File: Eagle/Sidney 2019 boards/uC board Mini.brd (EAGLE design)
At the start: 100 x 100 mm, 55 parts

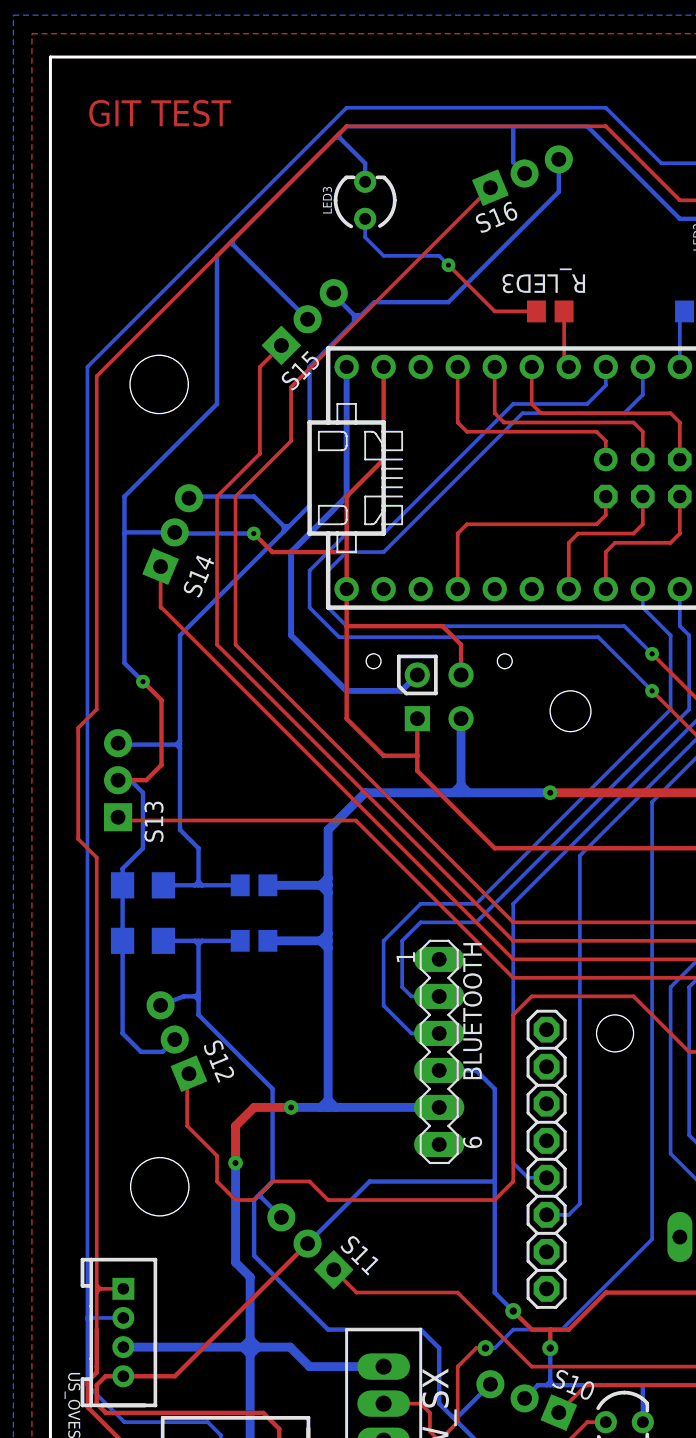
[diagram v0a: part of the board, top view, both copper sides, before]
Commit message: slight improvements on the top PCB
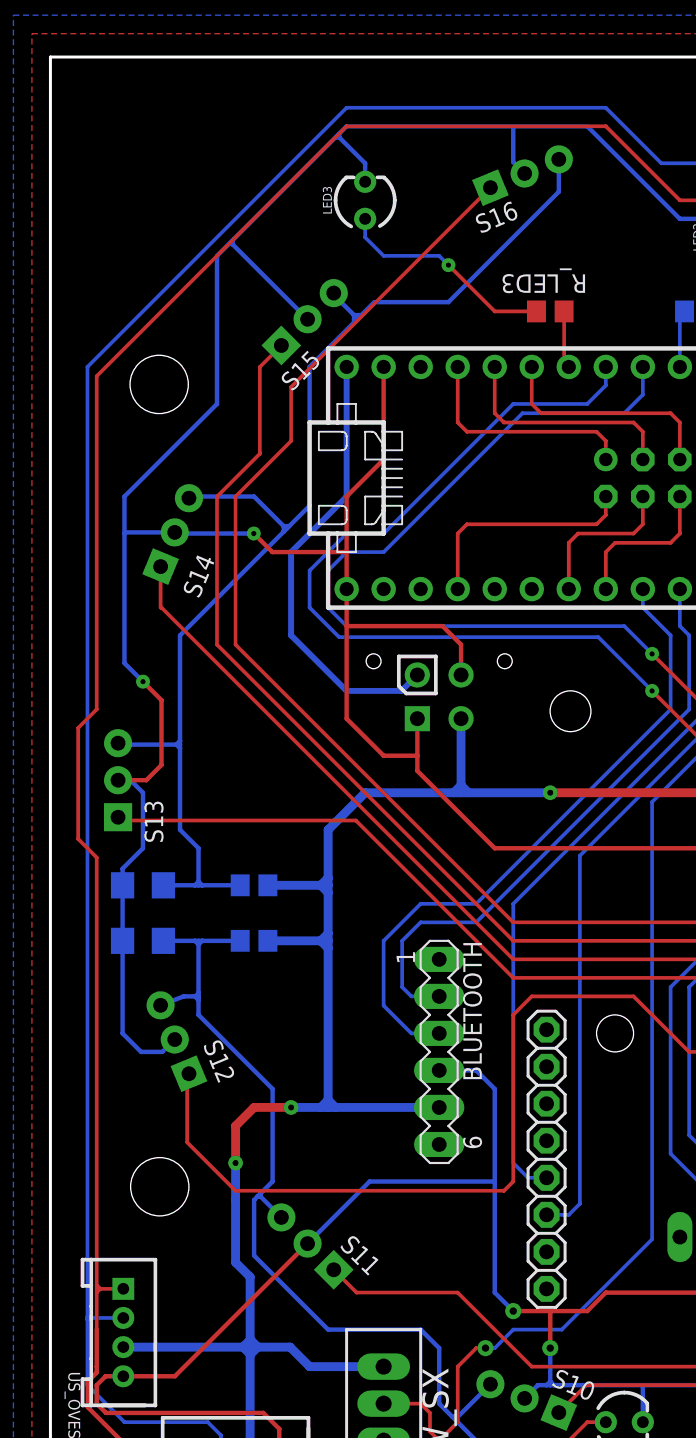
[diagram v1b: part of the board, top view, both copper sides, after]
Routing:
- net SP12: track 86.2 -> 84.3 mm
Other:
- board text removed: "GIT TEST"
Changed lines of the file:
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@@
 <text x="31.75" y="49.53" size="1.778" layer="26" rot="MR0">SUPPLY_CON</text>
 <text x="64.77" y="64.77" size="1.778" layer="25">TEENSY 3.5</text>
-<text x="2.54" y="95.25" size="1.778" layer="1">GIT TEST</text>
 </plain>
 <attributes>
@@
 <wire x1="30.48" y1="15.24" x2="31.75" y2="13.97" width="0.3048" layer="16"/>
 <via x="31.75" y="13.97" extent="1-16" drill="0.5"/>
-<wire x1="31.75" y1="13.97" x2="33.02" y2="12.7" width="0.3048" layer="1"/>
 <wire x1="50.8" y1="19.05" x2="50.8" y2="15.24" width="0.3048" layer="1"/>
 <wire x1="30.48" y1="22.86" x2="30.48" y2="15.24" width="0.3048" layer="16"/>
-<wire x1="35.56" y1="12.7" x2="34.29" y2="12.7" width="0.3048" layer="1"/>
-<wire x1="34.29" y1="12.7" x2="33.02" y2="12.7" width="0.3048" layer="1"/>
 <wire x1="66.294" y1="15.494" x2="66.04" y2="15.24" width="0.3048" layer="1"/>
 <wire x1="66.04" y1="15.24" x2="60.96" y2="15.24" width="0.3048" layer="1"/>
 <wire x1="60.96" y1="15.24" x2="50.8" y2="15.24" width="0.3048" layer="1"/>
-<wire x1="38.1" y1="15.24" x2="35.56" y2="12.7" width="0.3048" layer="1"/>
+<wire x1="38.1" y1="15.24" x2="36.83" y2="13.97" width="0.3048" layer="1"/>
 <wire x1="50.8" y1="15.24" x2="38.1" y2="15.24" width="0.3048" layer="1"/>
-<wire x1="34.29" y1="12.7" x2="34.29" y2="11.43" width="0.3048" layer="1"/>
 <via x="34.29" y="11.43" extent="1-16" drill="0.5"/>
 <wire x1="34.29" y1="11.43" x2="34.29" y2="9.144" width="0.3048" layer="16"/>
@@
 <vertex x="-2.54" y="-1.27"/>
 </polygon>
+<wire x1="31.75" y1="13.97" x2="34.29" y2="13.97" width="0.3048" layer="1"/>
+<wire x1="34.29" y1="13.97" x2="36.83" y2="13.97" width="0.3048" layer="1"/>
+<wire x1="34.29" y1="11.43" x2="34.29" y2="13.97" width="0.3048" layer="1"/>
 </signal>
 <signal name="SP3">
@@
 <wire x1="54.61" y1="31.75" x2="43.815" y2="31.75" width="0.254" layer="1"/>
 <wire x1="33.02" y1="35.56" x2="31.75" y2="34.29" width="0.254" layer="1"/>
-<wire x1="31.75" y1="34.29" x2="31.75" y2="22.86" width="0.254" layer="1"/>
-<wire x1="31.75" y1="22.86" x2="30.48" y2="21.59" width="0.254" layer="1"/>
-<wire x1="30.48" y1="21.59" x2="19.05" y2="21.59" width="0.254" layer="1"/>
-<wire x1="19.05" y1="21.59" x2="17.78" y2="22.86" width="0.254" layer="1"/>
-<wire x1="17.78" y1="22.86" x2="15.24" y2="22.86" width="0.254" layer="1"/>
+<wire x1="31.75" y1="22.86" x2="31.75" y2="34.29" width="0.254" layer="1"/>
 <wire x1="43.815" y1="31.75" x2="40.005" y2="35.56" width="0.254" layer="1"/>
 <wire x1="40.005" y1="35.56" x2="33.02" y2="35.56" width="0.254" layer="1"/>
-<wire x1="13.97" y1="21.59" x2="15.24" y2="22.86" width="0.254" layer="1"/>
-<wire x1="12.7" y1="21.59" x2="13.97" y2="21.59" width="0.254" layer="1"/>
-<wire x1="9.3824" y1="30.133725" x2="9.50201875" y2="30.25334375" width="0.254" layer="1"/>
-<wire x1="9.3824" y1="30.133725" x2="9.3824" y2="26.67" width="0.254" layer="1"/>
-<wire x1="9.3824" y1="26.67" x2="11.43" y2="24.6224" width="0.254" layer="1"/>
-<wire x1="11.43" y1="24.6224" x2="11.43" y2="22.86" width="0.254" layer="1"/>
-<wire x1="11.43" y1="22.86" x2="12.7" y2="21.59" width="0.254" layer="1"/>
+<wire x1="9.50201875" y1="30.25334375" x2="9.3824" y2="30.133725" width="0.254" layer="1"/>
+<wire x1="31.115" y1="22.225" x2="31.75" y2="22.86" width="0.254" layer="1"/>
+<wire x1="9.3824" y1="30.133725" x2="9.3824" y2="25.5426" width="0.254" layer="1"/>
+<wire x1="9.3824" y1="25.5426" x2="12.7" y2="22.225" width="0.254" layer="1"/>
+<wire x1="12.7" y1="22.225" x2="31.115" y2="22.225" width="0.254" layer="1"/>
 </signal>
 <signal name="SP1">
@@
 <wire x1="90.17" y1="95.885" x2="89.7255" y2="96.3295" width="0.6096" layer="16"/>
 <wire x1="89.7255" y1="96.3295" x2="89.535" y2="96.52" width="0.6096" layer="16"/>
-<wire x1="12.7" y1="17.31" x2="12.7" y2="24.13" width="0.6096" layer="16"/>
+<wire x1="12.7" y1="17.31" x2="12.7" y2="21.59" width="0.6096" layer="16"/>
+<wire x1="12.7" y1="21.59" x2="12.7" y2="24.13" width="0.6096" layer="16"/>
 <wire x1="13.97" y1="27.94" x2="12.7" y2="26.67" width="0.6096" layer="1"/>
 <via x="12.7" y="24.13" extent="1-16" drill="0.4064"/>

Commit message: backup
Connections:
- removed net +5V/1: ARDUINO_PRO_MINI.21, BLUETOOTH.5, IMU_1.1, RB1.1, RB2.1, RB3.1, RB4.1, R_SCL.2, R_SCL1.2, R_SDA.2, R_SDA1.2, SUPPLY_CON.P$2, SW_DX.1, SW_SX.1, U$2.27, US_EST.3, US_NORD.3, US_OVEST.3, US_SUD.3
- new net +5V/S: RB1.1, RB2.1, RB3.1, RB4.1, R_SCL1.2, R_SDA1.2, SUPPLY_CON.P$2, SW_DX.1, SW_SX.1, US_EST.3, US_NORD.3, US_OVEST.3, US_SUD.3
- net +5V: now also ARDUINO_PRO_MINI.21, BLUETOOTH.5, IMU_1.1, R_SCL.2, R_SDA.2, U$2.27
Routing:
- net +5V/1: track 368.8 -> 0.00 mm, vias 10 -> 0
- net +5V/S: track 0.00 -> 350.4 mm, vias 0 -> 10

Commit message: general improvements to the boards
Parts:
- removed SUPPLY_CON: (no value), con-molex-micro-fit-3_0:43045-0412
- added J1: 39-28-1043, 39-28-1043:39-28-1043
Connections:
- net +5V: now also J1.3; no longer SUPPLY_CON.P$3
- net +5V/S: now also J1.2; no longer SUPPLY_CON.P$2
- net GND: now also J1.1, J1.4; no longer SUPPLY_CON.P$1, SUPPLY_CON.P$4
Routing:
- net GND: track 657.9 -> 653.3 mm
- net +5V/S: track 350.4 -> 345.8 mm
- net +5V: track 30.7 -> 29.1 mm
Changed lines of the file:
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@@
 <attribute name="SPICEPREFIX" value="R" x="88.9" y="92.075" size="1.778" layer="27" rot="R90" display="off"/>
 </element>
-<element name="SUPPLY_CON" library="con-molex-micro-fit-3_0" package="43045-0412" value="" x="26.67" y="54.61" smashed="yes" rot="MR0"/>
 <element name="R_BALL" library="rcl" library_urn="urn:adsk.eagle:library:334" package="R1206" package3d_urn="urn:adsk.eagle:package:23540/2" value="330" x="90.17" y="41.91" smashed="yes" rot="MR0">
 <attribute name="NAME" x="87.63" y="43.18" size="1.27" layer="25"/>
 <attribute name="SPICEPREFIX" value="R" x="90.17" y="41.91" size="1.778" layer="28" rot="MR0" display="off"/>
 <attribute name="VALUE" x="88.9" y="39.37" size="1.27" layer="27"/>
+</element>
+<element name="J1" library="39-28-1043" package="39-28-1043" value="39-28-1043" x="27.94" y="50.8" smashed="yes" rot="MR0">
+<attribute name="DESCRIPTION" value="Mini-Fit Jr. Vertical Header, 4.20mm Pitch, Dual Row, 4 Circuits, without Snap-in Plastic Peg PCB Lock, Tin, Natural" x="27.94" y="50.8" size="1.778" layer="28" rot="MR0" display="off"/>
+<attribute name="HEIGHT" value="mm" x="27.94" y="50.8" size="1.778" layer="28" rot="MR0" display="off"/>
+<attribute name="MANUFACTURER_NAME" value="Molex" x="27.94" y="50.8" size="1.778" layer="28" rot="MR0" display="off"/>
+<attribute name="MANUFACTURER_PART_NUMBER" value="39-28-1043" x="27.94" y="50.8" size="1.778" layer="28" rot="MR0" display="off"/>
+<attribute name="MOUSER_PART_NUMBER" value="538-39-28-1043" x="27.94" y="50.8" size="1.778" layer="28" rot="MR0" display="off"/>
+<attribute name="MOUSER_PRICE-STOCK" value="https://www.mouser.com/Search/Refine.aspx?Keyword=538-39-28-1043" x="27.94" y="50.8" size="1.778" layer="28" rot="MR0" display="off"/>
+<attribute name="RS_PART_NUMBER" value="4841899P" x="27.94" y="50.8" size="1.778" layer="28" rot="MR0" display="off"/>
+<attribute name="RS_PRICE-STOCK" value="http://uk.rs-online.com/web/p/products/4841899P" x="27.94" y="50.8" size="1.778" layer="28" rot="MR0" display="off"/>
 </element>
 </elements>
@@
 <contactref element="SW_DX" pad="3"/>
 <contactref element="LED_SW_DX" pad="K"/>
-<contactref element="SUPPLY_CON" pad="P$4"/>
-<contactref element="SUPPLY_CON" pad="P$1"/>
-<wire x1="28.17" y1="57.61" x2="28.17" y2="59.69" width="0.3048" layer="1"/>
 <wire x1="28.17" y1="59.69" x2="26.9" y2="60.96" width="0.3048" layer="1"/>
 <wire x1="26.9" y1="60.96" x2="20.32" y2="60.96" width="0.3048" layer="1"/>
@@
 <wire x1="69.85" y1="45.72" x2="66.04" y2="41.91" width="0.3048" layer="1"/>
 <wire x1="57.15" y1="41.91" x2="55.88" y2="43.18" width="0.3048" layer="1"/>
-<wire x1="25.17" y1="54.61" x2="25.17" y2="52.07" width="0.3048" layer="1"/>
 <wire x1="25.17" y1="52.07" x2="25.17" y2="51.03" width="0.3048" layer="1"/>
 <wire x1="30.48" y1="45.72" x2="55.88" y2="45.72" width="0.3048" layer="1"/>
@@
 <wire x1="34.29" y1="13.97" x2="36.83" y2="13.97" width="0.3048" layer="1"/>
 <wire x1="34.29" y1="11.43" x2="34.29" y2="13.97" width="0.3048" layer="1"/>
+<contactref element="J1" pad="1"/>
+<contactref element="J1" pad="4"/>
+<wire x1="25.84" y1="52.65" x2="3.175" y2="7.62" width="0" layer="19" extent="1-1"/>
+<wire x1="30.04" y1="58.15" x2="25.84" y2="52.65" width="0" layer="19" extent="1-1"/>
 </signal>
 <signal name="SP3">
@@
 <signal name="+5V">
 <contactref element="TEENSY_3.5" pad="VIN"/>
-<contactref element="SUPPLY_CON" pad="P$3"/>
-<wire x1="25.17" y1="57.61" x2="24.075" y2="56.515" width="0.4064" layer="16"/>
 <wire x1="24.075" y1="56.515" x2="20.32" y2="56.515" width="0.4064" layer="16"/>
 <wire x1="20.32" y1="56.515" x2="16.51" y2="60.325" width="0.4064" layer="16"/>
@@
 <contactref element="IMU_1" pad="1"/>
 <contactref element="ARDUINO_PRO_MINI" pad="21"/>
+<contactref element="J1" pad="3"/>
 <wire x1="66.294" y1="18.034" x2="86.36" y2="45.72" width="0" layer="19" extent="1-1"/>
 <wire x1="55.88" y1="19.05" x2="66.294" y2="18.034" width="0" layer="19" extent="1-1"/>
@@
 <wire x1="26.67" y1="27.94" x2="53.655" y2="15.24" width="0" layer="19" extent="16-16"/>
 <wire x1="24.075" y1="56.515" x2="26.67" y2="27.94" width="0" layer="19" extent="16-16"/>
+<wire x1="30.04" y1="52.65" x2="26.67" y2="27.94" width="0" layer="19" extent="1-1"/>
 </signal>
 <signal name="TX3">
@@
 <contactref element="SW_SX" pad="1"/>
 <contactref element="SW_DX" pad="1"/>
-<contactref element="SUPPLY_CON" pad="P$2"/>
 <contactref element="R_SDA1" pad="2"/>
 <contactref element="R_SCL1" pad="2"/>
@@
 <via x="12.7" y="24.13" extent="1-16" drill="0.4064"/>
 <wire x1="12.7" y1="26.67" x2="12.7" y2="24.13" width="0.6096" layer="1"/>
-<wire x1="28.17" y1="54.61" x2="28.17" y2="50.038" width="0.6096" layer="16"/>
 <wire x1="28.17" y1="49.53" x2="28.17" y2="50.038" width="0.6096" layer="16"/>
 <wire x1="22.86" y1="49.53" x2="27.662" y2="49.53" width="0.6096" layer="16"/>
@@
 <via x="17.78" y="27.94" extent="1-16" drill="0.4064"/>
 <wire x1="17.78" y1="27.94" x2="13.97" y2="27.94" width="0.6096" layer="1"/>
+<contactref element="J1" pad="2"/>
+<wire x1="25.84" y1="58.15" x2="5" y2="11.5" width="0" layer="19" extent="1-1"/>
 </signal>
 </signals>
